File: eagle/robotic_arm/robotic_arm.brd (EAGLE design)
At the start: 83.8 x 63.5 mm, 98 parts, among them J2 (ID,OD)=(2.1,5.5)MM, SW1 5A/28V, Y1 16MHz

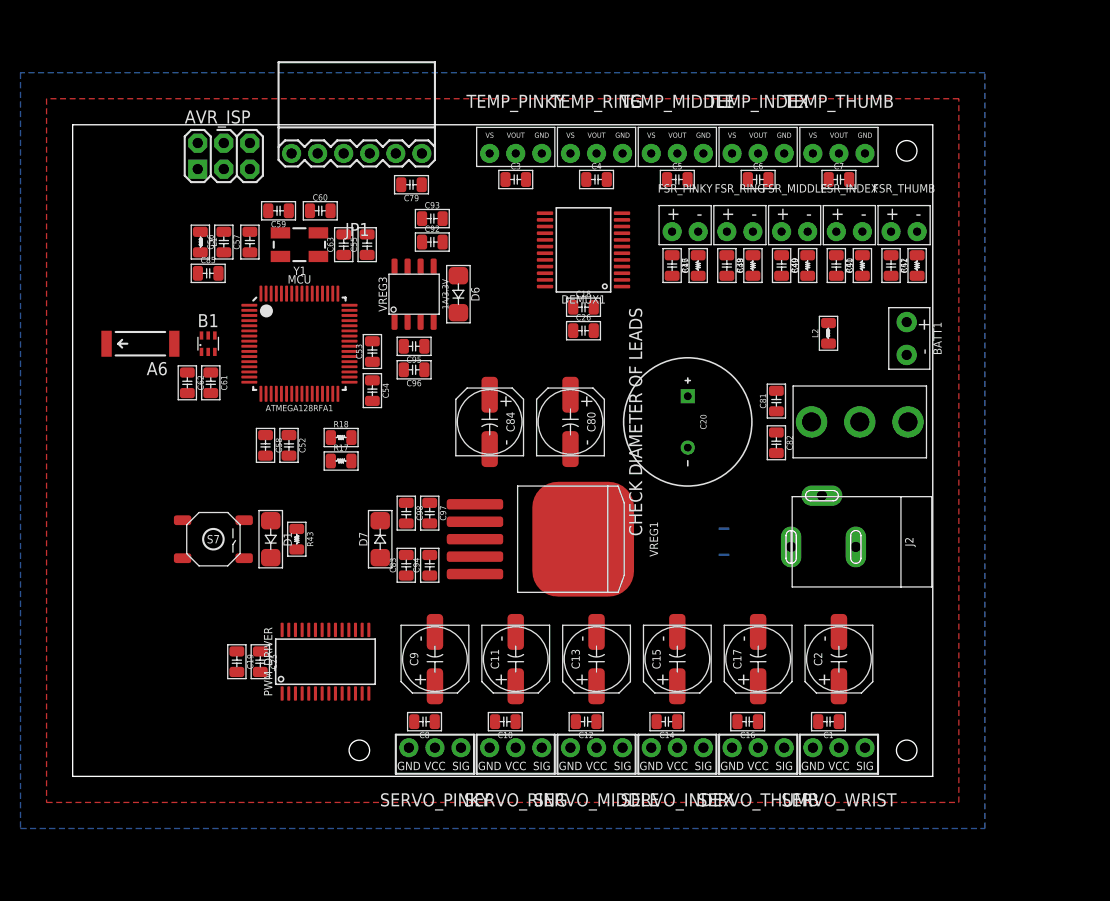
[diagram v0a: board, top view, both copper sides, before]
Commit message: Rev 1: Robotic Arm.  Initial placement of board with passive components on bottom side of board 3.20x2.50 inches (81.28x63.50mm)
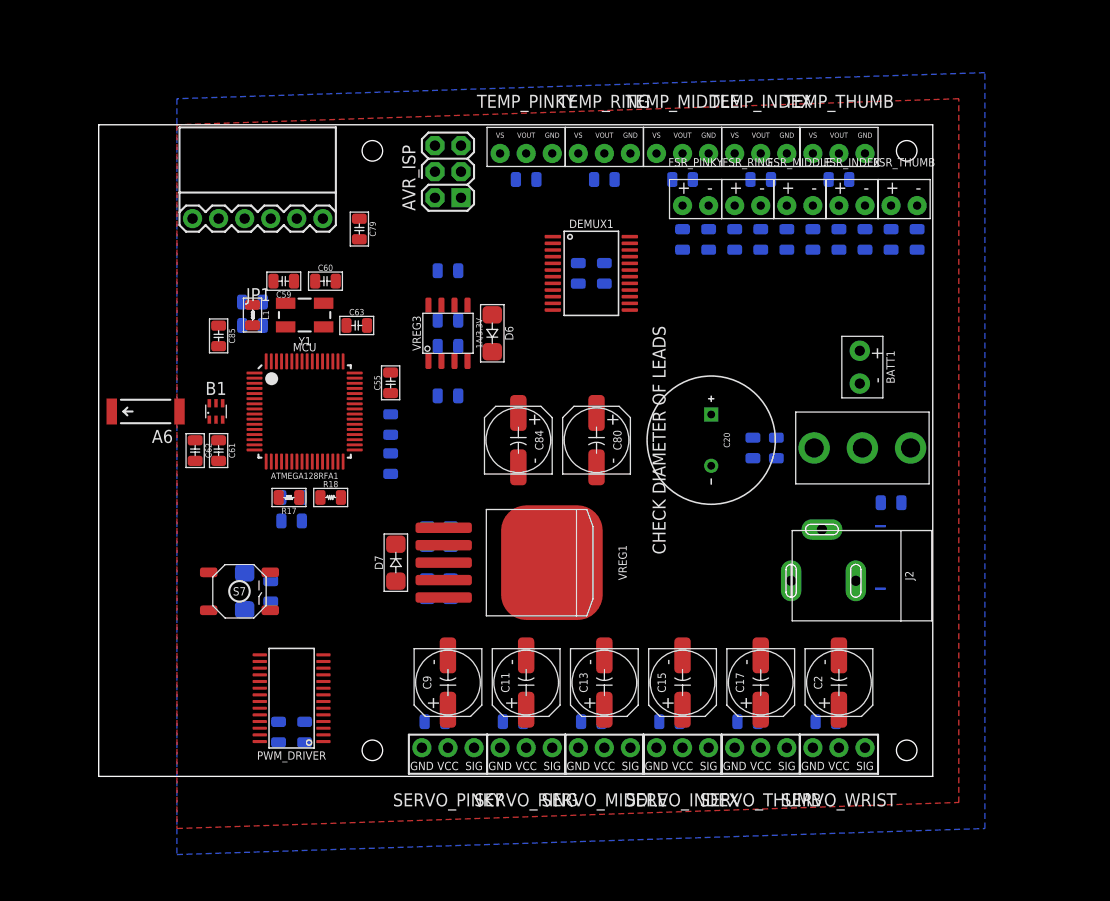
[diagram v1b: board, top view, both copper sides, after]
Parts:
- moved AVR_ISP 21.9 mm to (36.6, 58.9), turned to 90 degrees
- moved L2 17.6 mm to (79.8, 26.7), flipped to the bottom, turned to 0 degrees
- moved U$1 15.6 mm to (78.7, 18.3)
- moved U$2 15.2 mm to (78.7, 24.4)
- moved C55 13.7 mm to (31.0, 38.4)
- moved JP1 11.6 mm to (24.4, 54.4)
- moved C19 9.52 mm to (22.6, 4.32), flipped to the bottom, turned to 90 degrees
- moved L1 8.74 mm to (17.5, 45.0)
- moved C56 8.59 mm to (17.5, 43.9), flipped to the bottom, turned to 0 degrees
- moved C63 7.98 mm to (27.7, 43.9), turned to 0 degrees
- moved C58 7.79 mm to (21.3, 24.9), flipped to the bottom, turned to 180 degrees
- moved C92 7.77 mm to (36.6, 44.5), flipped to the bottom
- moved C53 7.33 mm to (31.0, 34.3), flipped to the bottom
- moved C54 7.33 mm to (31.0, 30.5), flipped to the bottom
- moved C25 7.08 mm to (20.1, 4.32), flipped to the bottom, turned to 90 degrees
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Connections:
- net GND: no longer C83.2, C94.2, C97.2, C98.2, VREG1.3, VREG1.TAB
- net NGND: now also C83.2, C94.2, C97.2, C98.2, VREG1.3, VREG1.TAB
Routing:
- added copper zone on layer 1, net NGND
- removed copper zone on layer 1, net GND
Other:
- board size 83.8 x 63.5 mm -> 81.3 x 63.5 mm

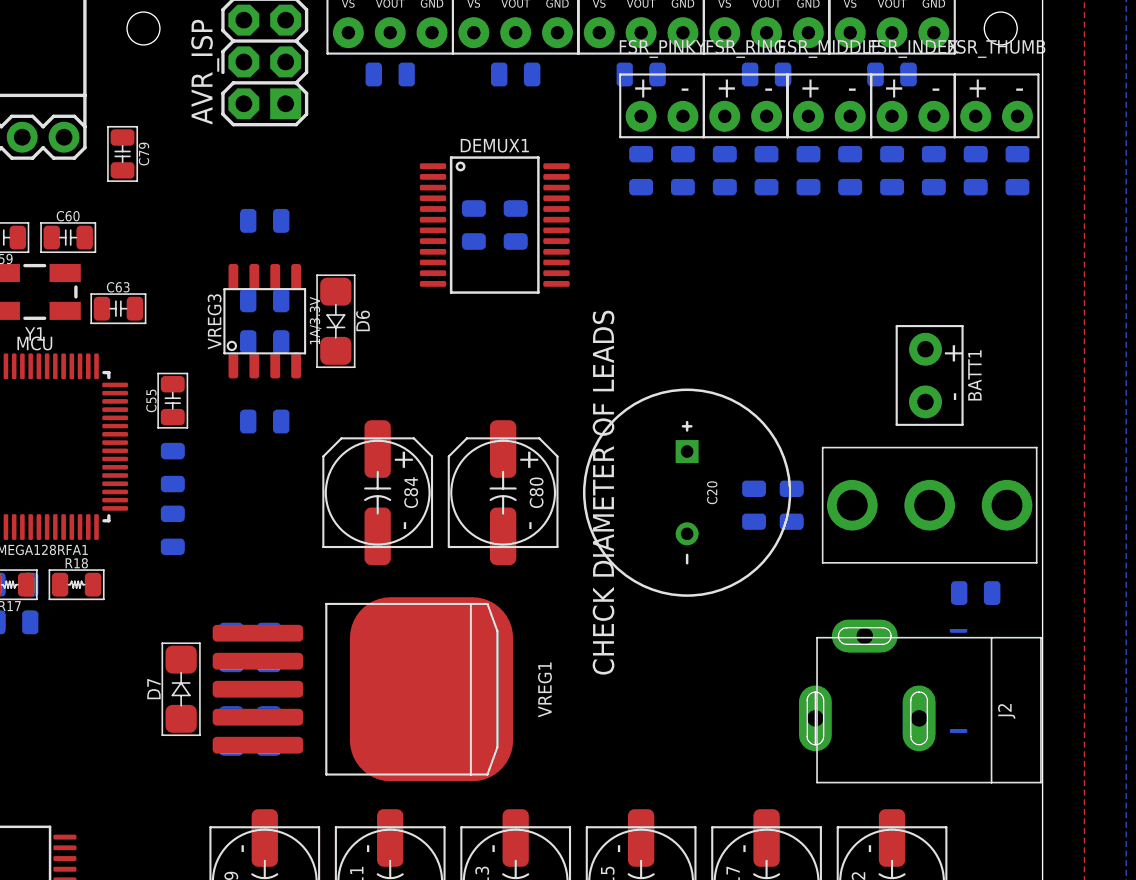
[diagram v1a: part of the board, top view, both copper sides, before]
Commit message: Rev 1: Robotic Arm.  Initial placement of board with passive components on bottom side.
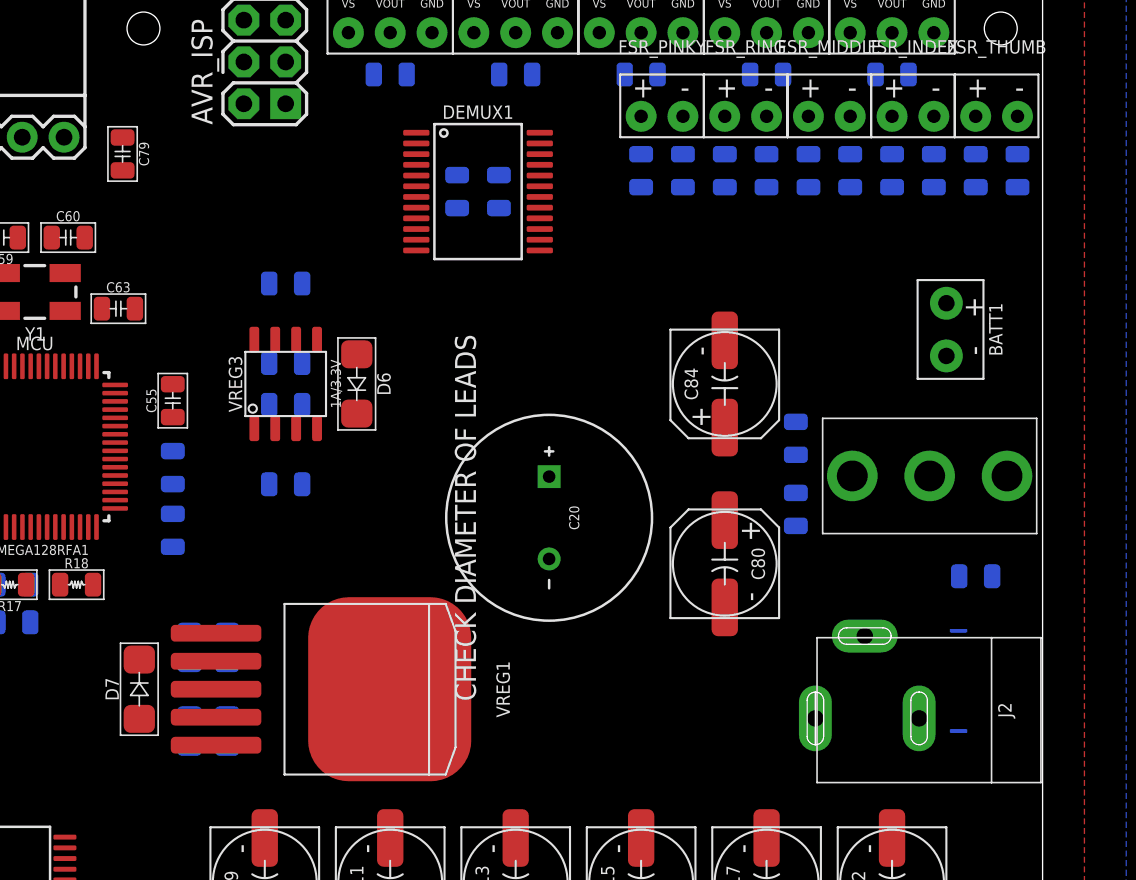
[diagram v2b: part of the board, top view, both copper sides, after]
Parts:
- moved C84 22.1 mm to (64.5, 39.4), turned to 90 degrees
- moved C80 14.1 mm to (64.5, 28.4)
- moved C20 8.52 mm to (53.8, 31.2)
- moved C81 4.79 mm to (68.8, 36.1), turned to 90 degrees
- moved D6 4.02 mm to (42.2, 39.4)
- moved C92 4.02 mm to (37.8, 40.6)
- moved C93 4.02 mm to (37.8, 45.5)
- moved C96 4.02 mm to (37.8, 33.3)
- moved VREG3 4.02 mm to (37.8, 39.4)
- moved C95 4.02 mm to (37.8, 38.1)
- moved BATT1 3.07 mm to (78.0, 42.7)
- moved C83 2.54 mm to (32.0, 18.3)
- moved C94 2.54 mm to (34.3, 18.3)
- moved C97 2.54 mm to (34.3, 23.4)
- moved C98 2.54 mm to (32.0, 23.4)
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
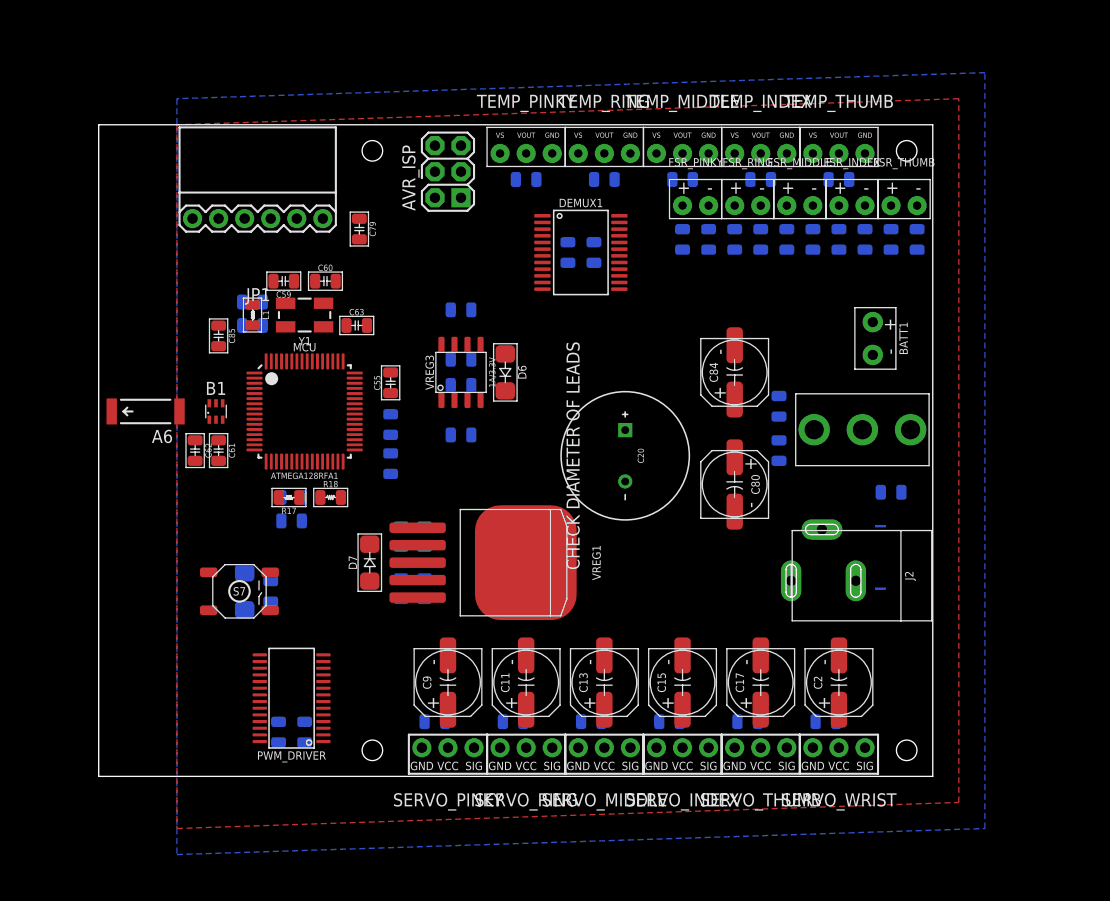
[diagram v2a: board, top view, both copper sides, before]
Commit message: Routed NGND plane + 5V plane + PWM Driver to SERVO sig traces.  Routed TEMP and FSR sig pins to DEMUX.
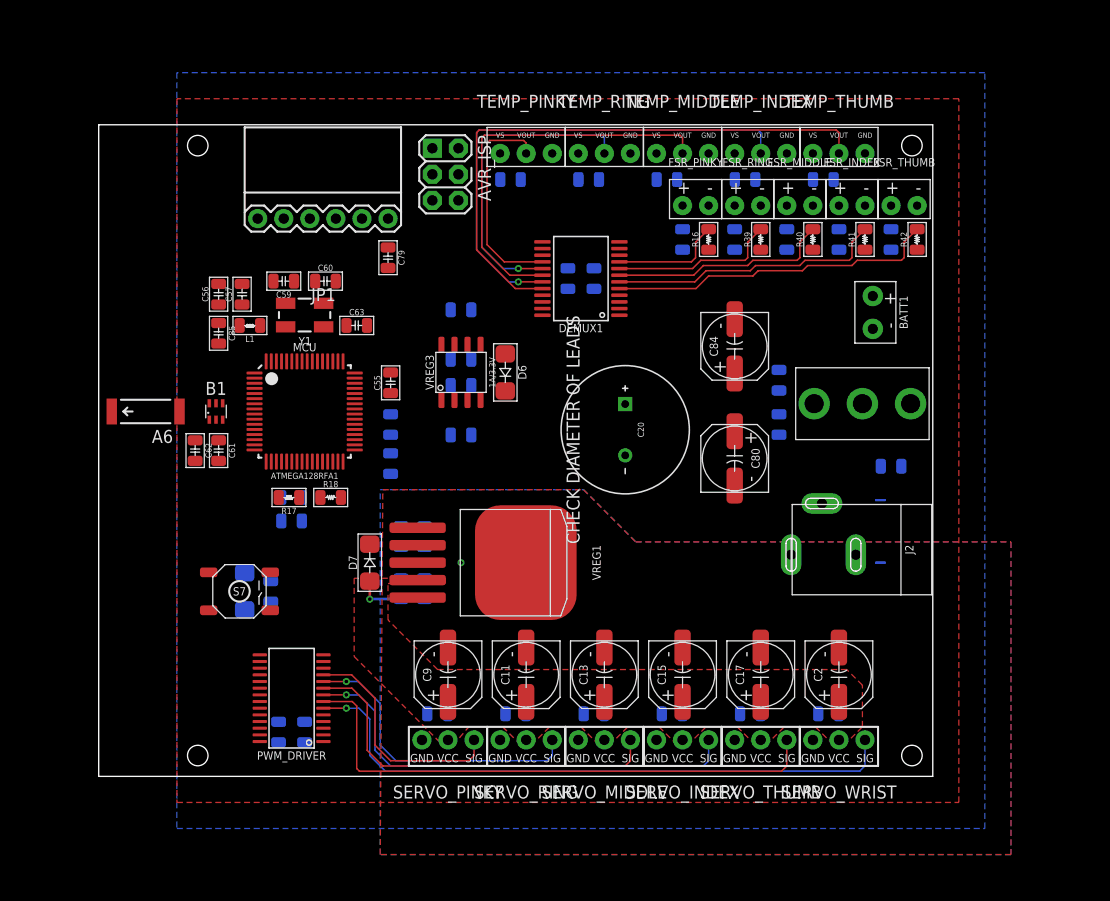
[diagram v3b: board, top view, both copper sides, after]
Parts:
- moved JP1 6.35 mm to (30.7, 54.4)
- moved C56 4.49 mm to (14.2, 47.0), flipped to the top, turned to 90 degrees
- moved C79 3.95 mm to (30.7, 50.5)
- moved BATT1 2.54 mm to (78.0, 45.2)
- moved SW1 2.54 mm to (77.0, 36.3)
- moved C18 2.54 mm to (50.8, 48.5), turned to 90 degrees
- moved C26 2.54 mm to (48.3, 48.5), turned to 90 degrees
- moved C80 2.54 mm to (64.5, 31.0)
- moved C81 2.54 mm to (68.8, 38.6)
- moved C82 2.54 mm to (68.8, 34.3)
- moved C84 2.54 mm to (64.5, 41.9)
- moved DEMUX1 2.54 mm to (49.5, 48.5), turned to 180 degrees
- moved J2 2.54 mm to (76.2, 22.1)
- moved L2 2.54 mm to (79.8, 30.2)
- moved U$1 2.54 mm to (78.7, 20.8)
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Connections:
- net SERVO_INDEX: now also SERVO_MIDDLE.1; no longer SERVO_INDEX.1
- net SERVO_MIDDLE: now also SERVO_INDEX.1; no longer SERVO_MIDDLE.1
- net SERVO_PINKY: now also SERVO_WRIST.1; no longer SERVO_PINKY.1
- net SERVO_RING: now also SERVO_THUMB.1; no longer SERVO_RING.1
- net SERVO_THUMB: now also SERVO_RING.1; no longer SERVO_THUMB.1
- net SERVO_WRIST: now also SERVO_PINKY.1; no longer SERVO_WRIST.1
- net TEMP_INDEX: now also TEMP_RING.2; no longer TEMP_INDEX.2
- net TEMP_PINKY: now also TEMP_THUMB.2; no longer TEMP_PINKY.2
- net TEMP_RING: now also TEMP_INDEX.2; no longer TEMP_RING.2
- net TEMP_THUMB: now also TEMP_PINKY.2; no longer TEMP_THUMB.2
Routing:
- net SERVO_PINKY: track 0.00 -> 60.2 mm, vias 0 -> 1
- net TEMP_PINKY: track 0.00 -> 56.9 mm
- net SERVO_RING: track 0.00 -> 54.3 mm
- net TEMP_RING: track 0.00 -> 49.1 mm, vias 0 -> 1
- net SERVO_MIDDLE: track 0.00 -> 44.9 mm, vias 0 -> 1
- net TEMP_MIDDLE: track 0.00 -> 39.0 mm
- net SERVO_INDEX: track 0.00 -> 38.0 mm
- net FSR_THUMB: track 0.00 -> 32.3 mm
- net TEMP_INDEX: track 0.00 -> 31.1 mm, vias 0 -> 1
- net SERVO_THUMB: track 0.00 -> 29.6 mm, vias 0 -> 1
- net FSR_INDEX: track 0.00 -> 26.9 mm
- net SERVO_WRIST: track 0.00 -> 22.6 mm
- net FSR_MIDDLE: track 0.00 -> 21.6 mm
- net TEMP_THUMB: track 0.00 -> 21.0 mm
- net FSR_RING: track 0.00 -> 16.3 mm
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- added copper zone on layer 1, net 5V
- added copper zone on layer 1, net GND
- added copper zone on layer 16, net GND
- added copper zone on layer 16, net NGND
- removed copper zone on layer 16, net AGND

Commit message: Routed AVCC + AGND power planes
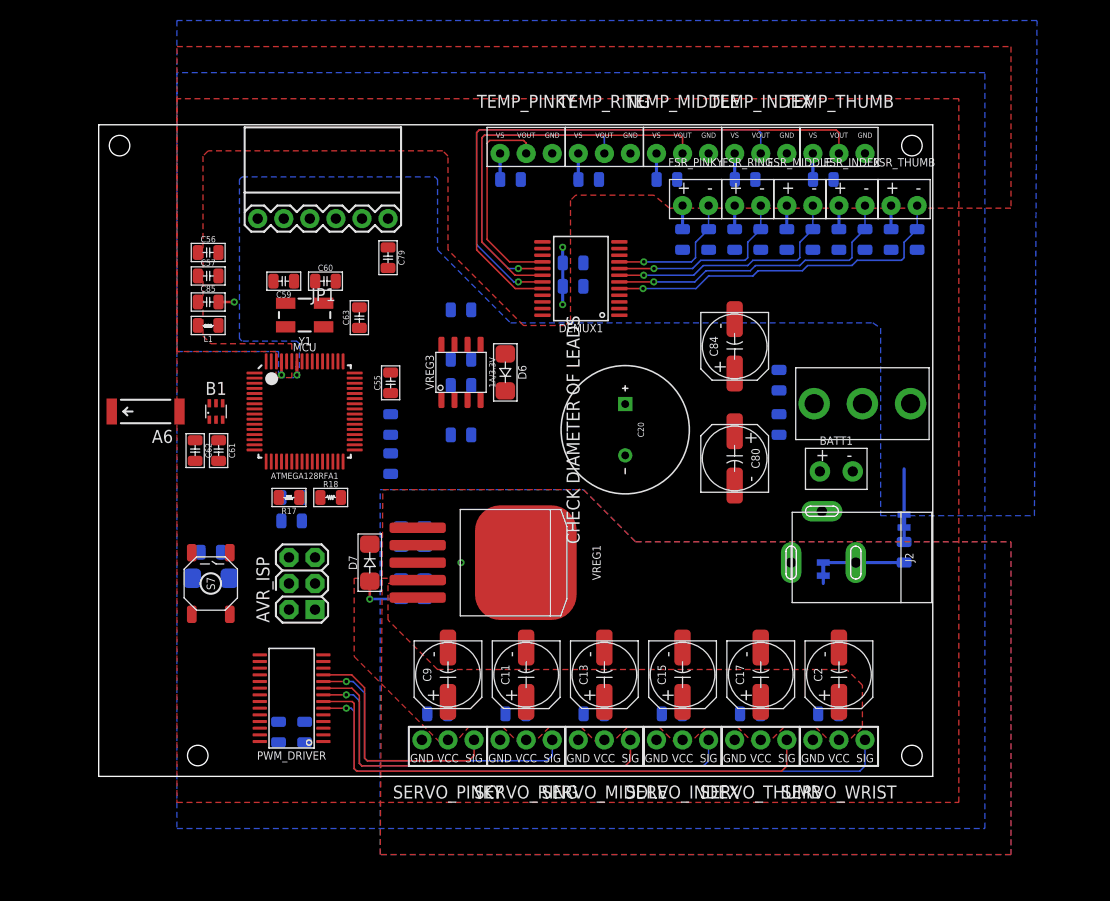
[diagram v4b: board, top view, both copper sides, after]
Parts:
- removed U$1, U$2: NET_BRIDGE, MrSwirlyEyes:NET_BRIDGE
- added SUPPLY51, SUPPLY52: 2PT_GND_TIE, SparkFun-PowerSymbols:2PT_GND_TIE
- moved AVR_ISP 42.3 mm to (22.4, 18.8), turned to 90 degrees
- moved BATT1 15.9 mm to (74.4, 29.7), turned to 0 degrees
- moved L2 8.48 mm to (81.0, 21.8), turned to 90 degrees
- moved R43 6.97 mm to (13.5, 21.8), turned to 180 degrees
- moved C56 4.19 mm to (13.2, 51.1), turned to 0 degrees
- moved L1 4.06 mm to (13.2, 43.9)
- moved C57 3.75 mm to (13.2, 48.8), turned to 0 degrees
- moved D1 3.54 mm to (13.5, 19.3), turned to 180 degrees
- moved C85 3.21 mm to (13.2, 46.2), turned to 0 degrees
- moved S7 2.90 mm to (13.5, 18.8), turned to 270 degrees
- moved C18 2.54 mm to (48.8, 50.0), turned to 180 degrees
- moved C26 0.92 mm to (48.8, 47.8), turned to 180 degrees
- moved C63 0.80 mm to (27.9, 44.7), turned to 90 degrees
- moved J2 0.76 mm to (76.2, 21.3)
- flipped R16 to the bottom
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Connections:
- net AGND: now also SUPPLY52.P$2; no longer U$2.P$2
- net GND: now also SUPPLY51.P$2; no longer U$1.P$2
- net N$38: now also SUPPLY52.P$1; no longer U$2.P$1
- net NGND: now also SUPPLY51.P$1; no longer U$1.P$1
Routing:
- net AVCC: track 0.00 -> 29.8 mm, vias 0 -> 2
- net AGND: track 0.00 -> 9.21 mm, vias 0 -> 3
- net GND: track 0.00 -> 7.87 mm
- net FSR_THUMB: track 32.3 -> 34.6 mm, vias 0 -> 1
- net FSR_RING: track 16.3 -> 18.6 mm, vias 0 -> 1
- net FSR_PINKY: track 10.9 -> 13.2 mm, vias 0 -> 1
- net FSR_MIDDLE: track 21.6 -> 23.9 mm, vias 0 -> 1
- net FSR_INDEX: track 26.9 -> 29.2 mm, vias 0 -> 1
- net N$38: track 0.00 -> 1.41 mm
- net SERVO_WRIST: track 22.6 -> 23.9 mm
- net SERVO_THUMB: track 29.6 -> 31.0 mm
- net SERVO_MIDDLE: track 44.9 -> 46.2 mm
- net SERVO_PINKY: track 60.2 -> 61.3 mm
- net SERVO_INDEX: track 38.0 -> 39.2 mm
- net NGND: track 0.00 -> 0.77 mm
- added copper zone on layer 16, net AGND
- added copper zone on layer 1, net AVCC

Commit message: Some more touches to AGND + AVCC power planes
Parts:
- moved C93 12.9 mm to (35.8, 32.8), turned to 270 degrees
- moved C96 10.2 mm to (48.0, 32.8), turned to 270 degrees
- moved C92 8.36 mm to (40.6, 32.8), turned to 270 degrees
- moved VREG3 7.75 mm to (41.9, 32.8), turned to 180 degrees
- moved C95 7.54 mm to (43.2, 32.8), turned to 270 degrees
- moved SW1 4.83 mm to (77.0, 41.1), turned to 90 degrees
- moved C82 3.88 mm to (66.8, 31.0)
- moved C81 3.25 mm to (66.8, 36.1)
- moved C84 3.05 mm to (64.5, 38.9)
- moved C80 2.79 mm to (64.5, 28.2)
- moved C20 2.54 mm to (53.8, 36.3), turned to 90 degrees
- moved D6 2.30 mm to (41.9, 37.1), turned to 0 degrees
- moved C18 0.76 mm to (49.5, 50.0)
- moved C26 0.76 mm to (49.5, 47.8)
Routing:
- net AGND: track 9.21 -> 13.3 mm, vias 3 -> 5
